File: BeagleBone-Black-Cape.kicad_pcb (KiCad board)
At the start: 4 copper layers, 61.9 x 92.1 mm, 60 parts, among them J501 Conn_ARM_JTAG_SWD_10, J502 3.3V, P101 BeagleBone_Black_Header, P102 BeagleBone_Black_Header, U401 LM3671, U601 cc1352p, Y601 32.768kHz, Y602 48MHz

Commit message: slowly but surely getting more things connected. trying to merge UI footprints. Standby
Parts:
- moved C603 35.4 mm to (158.6, 91.7)
- moved C604 33.2 mm to (158.6, 89.3)
- moved Y601 32.6 mm to (153.8, 90.6), turned to 90 degrees
- moved Y602 10.9 mm to (132.8, 88.7), turned to 90 degrees
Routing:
- net VDDR: track 0.00 -> 24.9 mm
- net VDDS: track 0.00 -> 23.5 mm
- net X32K_Q1: track 0.00 -> 16.6 mm
- net X32K_Q2: track 0.00 -> 16.0 mm
- net SKY_V1_20DBM: track 46.7 -> 56.8 mm
- net SKY_V2_SUB1G: track 29.5 -> 39.6 mm
- net SKY_V3_2G4: track 34.7 -> 44.5 mm
- net GND: track 59.1 -> 66.9 mm, vias 9 -> 11
- net X48M_N: track 0.00 -> 7.14 mm
- net X48M_P: track 0.00 -> 6.03 mm
- net MCU_LED_2: track 0.00 -> 3.71 mm
- net MCU_LED_1: track 0.00 -> 3.54 mm
- net RX_TX: track 22.5 -> 20.4 mm
- net Net-(C205-Pad2): track 11.3 -> 12.5 mm

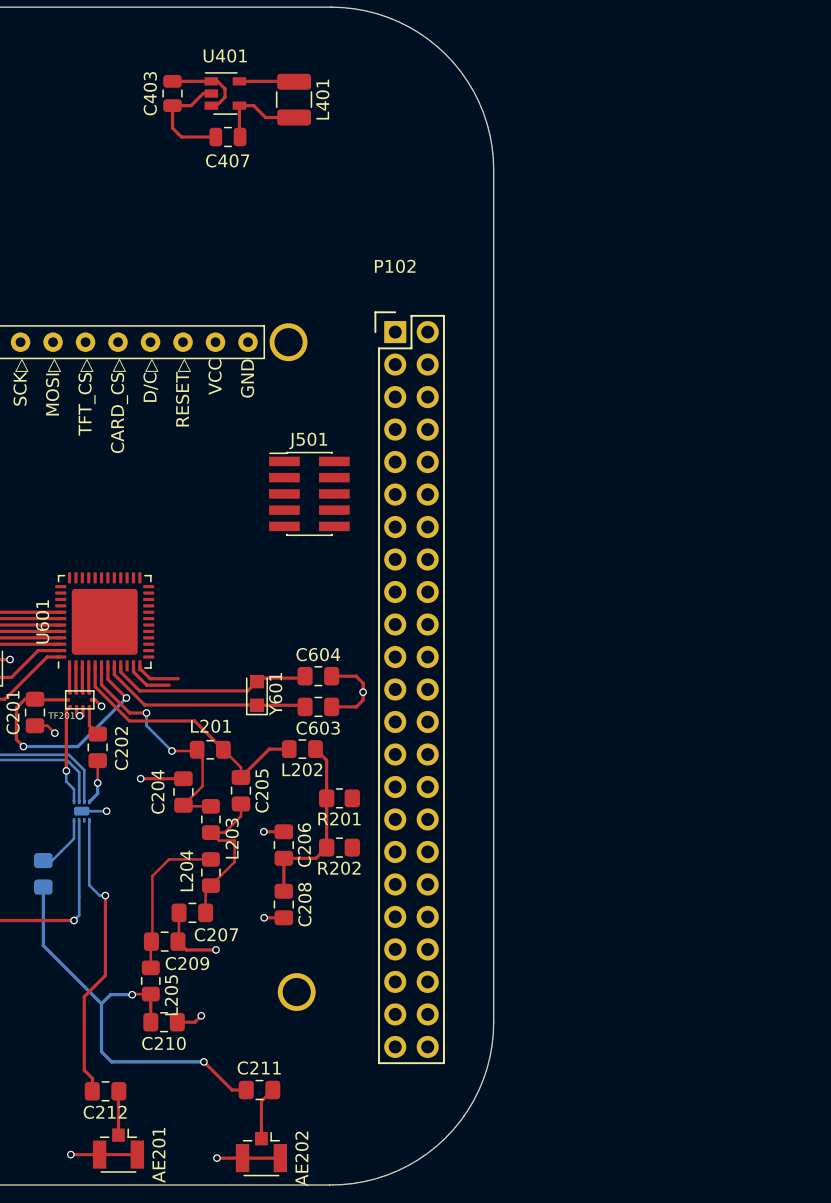
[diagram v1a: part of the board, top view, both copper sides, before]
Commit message: relinked LED and BTN footprints. Need to make flash symbol again
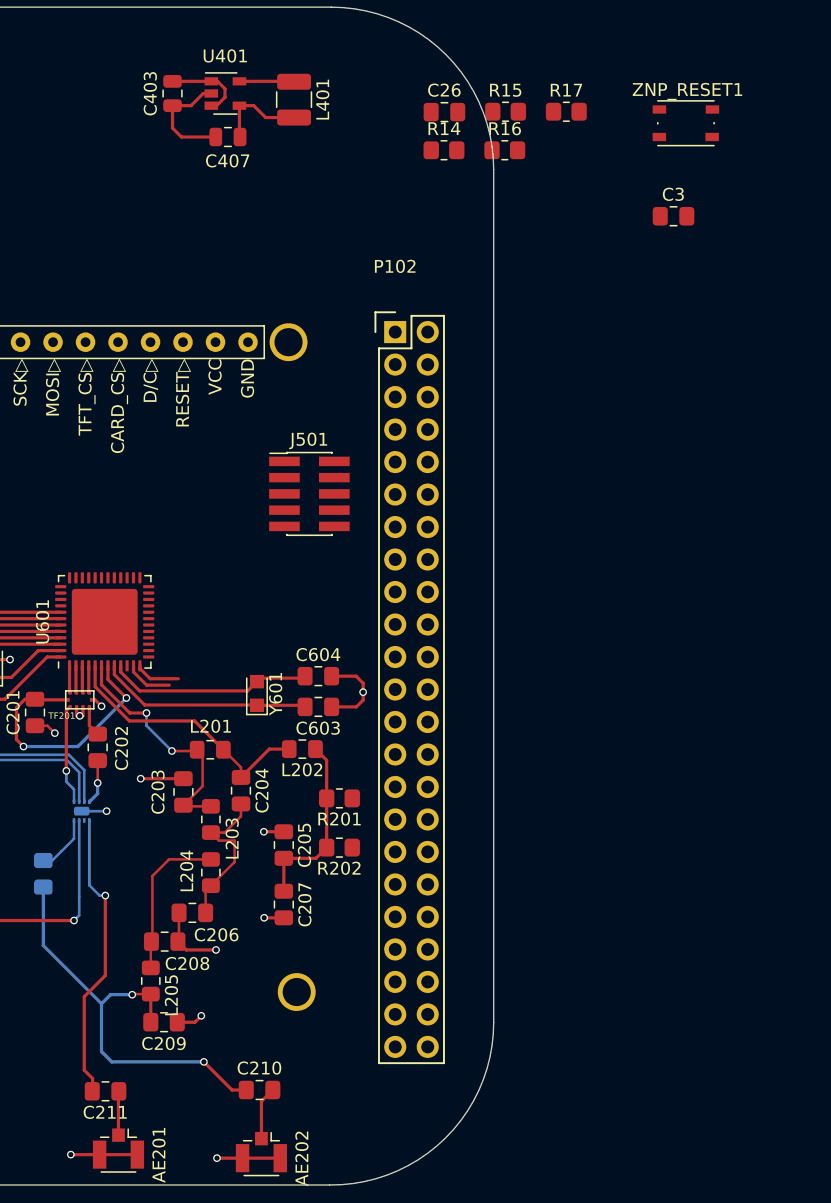
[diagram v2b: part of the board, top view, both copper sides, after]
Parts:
- added C26: 0.1u, Capacitor_SMD:C_0805_2012Metric_Pad1.18x1.45mm_HandSolder, F.Cu at (168.5, 45.2)
- added C3: 47pF, Capacitor_SMD:C_0805_2012Metric_Pad1.18x1.45mm_HandSolder, F.Cu at (186.4, 53.3)
- added R14: DNS, Resistor_SMD:R_0805_2012Metric_Pad1.20x1.40mm_HandSolder, F.Cu at (168.4, 48.2)
- added R15: DNS, Resistor_SMD:R_0805_2012Metric_Pad1.20x1.40mm_HandSolder, F.Cu at (173.3, 45.2)
- added R16: 2.2k, Resistor_SMD:R_0805_2012Metric_Pad1.20x1.40mm_HandSolder, F.Cu at (173.2, 48.2)
- added R17: 0, Resistor_SMD:R_0805_2012Metric_Pad1.20x1.40mm_HandSolder, F.Cu at (178.0, 45.2)
- added ZNP_RESET1: 612-LL3303F065QG, Button_Switch_SMD:SW_Push_1P1T_NO_Vertical_Wuerth_434133025816, F.Cu at (187.4, 46.1)
- renumbered C204 to C203, C205 to C204, C206 to C205, C207 to C206, C208 to C207, C209 to C208, C210 to C209, C211 to C210, C212 to C211, C213 to C212
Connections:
- C203 pad 2: RX_20dB_N -> TX_20dB_N
- L201 pad 2: RX_20dB_N -> TX_20dB_N
- L203 pad 1: RX_20dB_N -> TX_20dB_N
- R302 pad 1: (no net) -> Net-(R302-Pad1)
- U601 pad 30: (no net) -> Net-(R16-Pad2)
- U601 pad 6: RX_20dB_N -> (no net)

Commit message: more library nonsense
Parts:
- added BB_BTN_301: SW_Push, Button_Switch_SMD:SW_Push_1P1T_NO_Vertical_Wuerth_434133025816, F.Cu at (180.0, 83.5)
- added BB_BTN_302: SW_Push, Button_Switch_SMD:SW_Push_1P1T_NO_Vertical_Wuerth_434133025816, F.Cu at (180.0, 88.3)
- added BB_L_301: LED, LED_SMD:LED_0603_1608Metric_Pad1.05x0.95mm_HandSolder, F.Cu at (181.8, 70.0)
- added BB_L_302: LED, LED_SMD:LED_0603_1608Metric_Pad1.05x0.95mm_HandSolder, F.Cu at (181.8, 72.6)
- added MCU_L_301: LED, LED_SMD:LED_0603_1608Metric_Pad1.05x0.95mm_HandSolder, F.Cu at (186.2, 70.0)
- added MCU_L_302: LED, LED_SMD:LED_0603_1608Metric_Pad1.05x0.95mm_HandSolder, F.Cu at (186.2, 72.6)
- added PWR301: LED, LED_SMD:LED_0603_1608Metric_Pad1.05x0.95mm_HandSolder, F.Cu at (190.5, 70.0)
- added U3: MX25R8035FZUIL0, Package_SO:SOP-8_5.28x5.23mm_P1.27mm, F.Cu at (183.8, 98.0)
- added ZNP_BTN_301: SW_Push, Button_Switch_SMD:SW_Push_1P1T_NO_Vertical_Wuerth_434133025816, F.Cu at (186.7, 83.5)
- added ZNP_BTN_302: SW_Push, Button_Switch_SMD:SW_Push_1P1T_NO_Vertical_Wuerth_434133025816, F.Cu at (186.7, 88.3)
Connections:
- C3 pad 1: (no net) -> Net-(C3-Pad1)
- J501 pad 7: (no net) -> Net-(J501-Pad7)
- P101 pad 10: (no net) -> SYS_RESETN
- P101 pad 17: (no net) -> Net-(P101-Pad17)
- P101 pad 18: (no net) -> Net-(P101-Pad18)
- P101 pad 19: (no net) -> Net-(P101-Pad19)
- P101 pad 20: (no net) -> Net-(P101-Pad20)
- P101 pad 21: (no net) -> Net-(P101-Pad21)
- P101 pad 22: (no net) -> Net-(P101-Pad22)
- P101 pad 23: (no net) -> Net-(P101-Pad23)
- P101 pad 25: (no net) -> Net-(P101-Pad25)
- P101 pad 27: (no net) -> Net-(P101-Pad27)
- P101 pad 32: (no net) -> Net-(P101-Pad32)
- P101 pad 33: (no net) -> Net-(P101-Pad33)
- P101 pad 34: (no net) -> Net-(P101-Pad34)
- P101 pad 35: (no net) -> Net-(P101-Pad35)
- P101 pad 36: (no net) -> Net-(P101-Pad36)
- P101 pad 37: (no net) -> Net-(P101-Pad37)
- P101 pad 38: (no net) -> Net-(P101-Pad38)
- P101 pad 39: (no net) -> Net-(P101-Pad39)
- P101 pad 40: (no net) -> Net-(P101-Pad40)
- P101 pad 41: (no net) -> Net-(P101-Pad41)
- P101 pad 42: (no net) -> Net-(P101-Pad42)
- P101 pad 9: (no net) -> PWR_BTN
- P102 pad 10: (no net) -> Net-(P102-Pad10)
- P102 pad 11: (no net) -> Net-(P102-Pad11)
- P102 pad 12: (no net) -> Net-(P102-Pad12)
- P102 pad 13: (no net) -> Net-(P102-Pad13)
- P102 pad 14: (no net) -> Net-(P102-Pad14)
- P102 pad 15: (no net) -> Net-(P102-Pad15)
- P102 pad 16: (no net) -> Net-(P102-Pad16)
- P102 pad 17: (no net) -> Net-(P102-Pad17)
- P102 pad 18: (no net) -> Net-(P102-Pad18)
- P102 pad 19: (no net) -> Net-(P102-Pad19)
- P102 pad 20: (no net) -> Net-(P102-Pad20)
- P102 pad 21: (no net) -> Net-(P102-Pad21)
- P102 pad 22: (no net) -> Net-(P102-Pad22)
- P102 pad 23: (no net) -> Net-(P102-Pad23)
- P102 pad 24: (no net) -> Net-(P102-Pad24)
- P102 pad 25: (no net) -> Net-(P102-Pad25)
- P102 pad 26: (no net) -> Net-(P102-Pad26)
- P102 pad 27: (no net) -> Net-(P102-Pad27)
- P102 pad 28: (no net) -> Net-(P102-Pad28)
- P102 pad 29: (no net) -> Net-(P102-Pad29)
- P102 pad 3: (no net) -> Net-(P102-Pad3)
- P102 pad 30: (no net) -> Net-(P102-Pad30)
- P102 pad 31: (no net) -> Net-(P102-Pad31)
- P102 pad 32: (no net) -> Net-(P102-Pad32)
- P102 pad 33: (no net) -> Net-(P102-Pad33)
- P102 pad 34: (no net) -> Net-(P102-Pad34)
- P102 pad 35: (no net) -> Net-(P102-Pad35)
- P102 pad 36: (no net) -> Net-(P102-Pad36)
- P102 pad 37: (no net) -> Net-(P102-Pad37)
- P102 pad 38: (no net) -> Net-(P102-Pad38)
- P102 pad 39: (no net) -> Net-(P102-Pad39)
- P102 pad 4: (no net) -> Net-(P102-Pad4)
- P102 pad 40: (no net) -> Net-(P102-Pad40)
- P102 pad 41: (no net) -> Net-(P102-Pad41)
- P102 pad 42: (no net) -> Net-(P102-Pad42)
- P102 pad 43: (no net) -> Net-(P102-Pad43)
- P102 pad 44: (no net) -> Net-(P102-Pad44)
- P102 pad 45: (no net) -> Net-(P102-Pad45)
- P102 pad 46: (no net) -> Net-(P102-Pad46)
- P102 pad 5: (no net) -> Net-(P102-Pad5)
- P102 pad 6: (no net) -> Net-(P102-Pad6)
- P102 pad 7: (no net) -> Net-(P102-Pad7)
- P102 pad 8: (no net) -> Net-(P102-Pad8)
- P102 pad 9: (no net) -> Net-(P102-Pad9)
- R14 pad 2: (no net) -> Net-(R14-Pad2)
- R15 pad 2: (no net) -> Net-(R15-Pad2)
- R201 pad 1: (no net) -> Net-(R201-Pad1)
- R202 pad 1: (no net) -> Net-(R202-Pad1)
- R301 pad 2: (no net) -> Net-(PWR301-Pad2)
- R303 pad 2: (no net) -> Net-(MCU_L_301-Pad2)
- R304 pad 1: (no net) -> Net-(R304-Pad1)
- R305 pad 1: (no net) -> Net-(R305-Pad1)
- R306 pad 2: (no net) -> Net-(MCU_L_302-Pad2)
- R307 pad 2: (no net) -> Net-(BB_L_301-Pad2)
- R309 pad 2: (no net) -> Net-(BB_L_302-Pad2)
- TF202 pad 2: (no net) -> Net-(TF202-Pad2)
- TFT301 pad 6: (no net) -> Net-(TFT301-Pad6)
- U601 pad 10: (no net) -> Net-(U601-Pad10)
- U601 pad 14: (no net) -> Net-(U3-Pad2)
- U601 pad 15: (no net) -> Net-(U3-Pad5)
- U601 pad 16: (no net) -> Net-(U3-Pad6)
- U601 pad 17: (no net) -> Net-(U601-Pad17)
- U601 pad 28: (no net) -> Net-(U601-Pad28)
- U601 pad 29: (no net) -> Net-(U601-Pad29)
- U601 pad 31: (no net) -> Net-(U601-Pad31)
- U601 pad 32: (no net) -> Net-(U601-Pad32)
- U601 pad 36: (no net) -> Net-(U601-Pad36)
- U601 pad 37: (no net) -> Net-(U601-Pad37)
- U601 pad 38: (no net) -> Net-(U601-Pad38)
- U601 pad 39: (no net) -> Net-(U601-Pad39)
- U601 pad 40: (no net) -> Net-(U601-Pad40)
- U601 pad 6: (no net) -> RX_20dB_N

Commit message: prepped for PSU subsystem placements
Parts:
- C603: renamed from C26; moved to B.Cu
- R602: renamed from R14; moved to B.Cu
- R603: renamed from R15; moved to B.Cu
- R604: renamed from R16; moved to B.Cu
- R605: renamed from R17; moved to B.Cu
- U602: renamed from U3; moved to B.Cu
- moved R301 120.3 mm to (95.3, 70.1)
- moved R302 120.3 mm to (100.0, 76.0)
- moved R303 120.3 mm to (95.3, 73.1)
- moved R304 120.3 mm to (90.5, 70.1)
- moved R305 120.3 mm to (95.3, 76.0)
- moved R306 120.3 mm to (90.5, 73.1)
- moved R307 120.3 mm to (90.5, 76.0)
- moved R308 120.3 mm to (100.0, 70.1)
- moved R309 120.3 mm to (104.8, 76.0)
- moved R310 120.3 mm to (100.0, 73.1)
- moved C601 85.6 mm to (152.2, 53.4)
- moved C602 85.6 mm to (147.4, 53.4)
- moved R601 85.6 mm to (147.4, 50.4)
- moved C203 66.9 mm to (136.8, 98.2), turned to 90 degrees
- moved BB_BTN_301 62.0 mm to (133.9, 42.0), turned to 90 degrees
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- renumbered C3 to C203, C203 to C204, C204 to C205, C205 to C206, C206 to C207, C207 to C208, C208 to C209, C209 to C210, C210 to C211, C211 to C212, C212 to C213, C603 to C604, C604 to C605, ZNP_RESET1 to ZNP_RESET
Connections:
- C203 pad 1: Net-(C3-Pad1) -> Net-(C203-Pad1)
- C203 pad 2: Net-(C3-Pad2) -> Net-(C203-Pad2)
- J501 pad 7: Net-(J501-Pad7) -> (no net)
- P101 pad 10: SYS_RESETN -> (no net)
- P101 pad 17: Net-(P101-Pad17) -> (no net)
- P101 pad 18: Net-(P101-Pad18) -> (no net)
- P101 pad 19: Net-(P101-Pad19) -> (no net)
- P101 pad 20: Net-(P101-Pad20) -> (no net)
- P101 pad 21: Net-(P101-Pad21) -> (no net)
- P101 pad 22: Net-(P101-Pad22) -> (no net)
- P101 pad 23: Net-(P101-Pad23) -> (no net)
- P101 pad 25: Net-(P101-Pad25) -> (no net)
- P101 pad 27: Net-(P101-Pad27) -> (no net)
- P101 pad 32: Net-(P101-Pad32) -> (no net)
- P101 pad 33: Net-(P101-Pad33) -> (no net)
- P101 pad 34: Net-(P101-Pad34) -> (no net)
- P101 pad 35: Net-(P101-Pad35) -> (no net)
- P101 pad 36: Net-(P101-Pad36) -> (no net)
- P101 pad 37: Net-(P101-Pad37) -> (no net)
- P101 pad 38: Net-(P101-Pad38) -> (no net)
- P101 pad 39: Net-(P101-Pad39) -> (no net)
- P101 pad 40: Net-(P101-Pad40) -> (no net)
- P101 pad 41: Net-(P101-Pad41) -> (no net)
- P101 pad 42: Net-(P101-Pad42) -> (no net)
- P101 pad 9: PWR_BTN -> (no net)
- P102 pad 10: Net-(P102-Pad10) -> (no net)
- P102 pad 11: Net-(P102-Pad11) -> (no net)
- P102 pad 12: Net-(P102-Pad12) -> (no net)
- P102 pad 13: Net-(P102-Pad13) -> (no net)
- P102 pad 14: Net-(P102-Pad14) -> (no net)
- P102 pad 15: Net-(P102-Pad15) -> (no net)
- P102 pad 16: Net-(P102-Pad16) -> (no net)
- P102 pad 17: Net-(P102-Pad17) -> (no net)
- P102 pad 18: Net-(P102-Pad18) -> (no net)
- P102 pad 19: Net-(P102-Pad19) -> (no net)
- P102 pad 20: Net-(P102-Pad20) -> (no net)
- P102 pad 21: Net-(P102-Pad21) -> (no net)
- P102 pad 22: Net-(P102-Pad22) -> (no net)
- P102 pad 23: Net-(P102-Pad23) -> (no net)
- P102 pad 24: Net-(P102-Pad24) -> (no net)
- P102 pad 25: Net-(P102-Pad25) -> (no net)
- P102 pad 26: Net-(P102-Pad26) -> (no net)
- P102 pad 27: Net-(P102-Pad27) -> (no net)
- P102 pad 28: Net-(P102-Pad28) -> (no net)
- P102 pad 29: Net-(P102-Pad29) -> (no net)
- P102 pad 3: Net-(P102-Pad3) -> (no net)
- P102 pad 30: Net-(P102-Pad30) -> (no net)
- P102 pad 31: Net-(P102-Pad31) -> (no net)
- P102 pad 32: Net-(P102-Pad32) -> (no net)
- P102 pad 33: Net-(P102-Pad33) -> (no net)
- P102 pad 34: Net-(P102-Pad34) -> (no net)
- P102 pad 35: Net-(P102-Pad35) -> (no net)
- P102 pad 36: Net-(P102-Pad36) -> (no net)
- P102 pad 37: Net-(P102-Pad37) -> (no net)
- P102 pad 38: Net-(P102-Pad38) -> (no net)
- P102 pad 39: Net-(P102-Pad39) -> (no net)
- P102 pad 4: Net-(P102-Pad4) -> (no net)
- P102 pad 40: Net-(P102-Pad40) -> (no net)
- P102 pad 41: Net-(P102-Pad41) -> (no net)
- P102 pad 42: Net-(P102-Pad42) -> (no net)
- P102 pad 43: Net-(P102-Pad43) -> (no net)
- P102 pad 44: Net-(P102-Pad44) -> (no net)
- P102 pad 45: Net-(P102-Pad45) -> (no net)
- P102 pad 46: Net-(P102-Pad46) -> (no net)
- P102 pad 5: Net-(P102-Pad5) -> (no net)
- P102 pad 6: Net-(P102-Pad6) -> (no net)
- P102 pad 7: Net-(P102-Pad7) -> (no net)
- P102 pad 8: Net-(P102-Pad8) -> (no net)
- P102 pad 9: Net-(P102-Pad9) -> (no net)
- R201 pad 1: Net-(R201-Pad1) -> (no net)
- R202 pad 1: Net-(R202-Pad1) -> (no net)
- TF201 pad 1: Net-(C3-Pad2) -> Net-(C203-Pad2)
- TF202 pad 2: Net-(TF202-Pad2) -> (no net)
- TF202 pad 8: Net-(C3-Pad2) -> Net-(C203-Pad1)
- TFT301 pad 6: Net-(TFT301-Pad6) -> (no net)
- U601 pad 10: Net-(U601-Pad10) -> (no net)
- U601 pad 17: Net-(U601-Pad17) -> (no net)
- U601 pad 28: Net-(U601-Pad28) -> (no net)
- U601 pad 29: Net-(U601-Pad29) -> (no net)
- U601 pad 31: Net-(U601-Pad31) -> (no net)
- U601 pad 32: Net-(U601-Pad32) -> (no net)
- U601 pad 36: Net-(U601-Pad36) -> (no net)
- U601 pad 37: Net-(U601-Pad37) -> (no net)
- U601 pad 38: Net-(U601-Pad38) -> (no net)
- U601 pad 39: Net-(U601-Pad39) -> (no net)
- U601 pad 40: Net-(U601-Pad40) -> (no net)
- U601 pad 6: RX_20dB_N -> (no net)
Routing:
- net Net-(C3-Pad2): track 7.77 -> 0.00 mm, vias 1 -> 0
- net Net-(C203-Pad2): track 0.00 -> 7.48 mm
- net Net-(C203-Pad1): track 0.00 -> 5.03 mm, vias 0 -> 1
